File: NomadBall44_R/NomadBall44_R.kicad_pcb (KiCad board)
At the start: 2 copper layers, 144.8 x 96.5 mm, 48 parts, among them SW1 SW_Push, SW10 SW_Push, SW11 SW_Push, SW12 SW_Push, SW13 SW_Push, SW14 SW_Push, SW15 SW_Push, SW16 SW_Push, SW17 SW_Push, SW18 SW_Push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

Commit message: pmw3610のコネクタの位置を微調整
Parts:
- BT1: moved to B.Cu
- moved SW11 99.5 mm to (139.6, 59.1)
- moved SW17 99.5 mm to (139.6, 78.3)
- moved SW22 99.5 mm to (139.6, 97.4)
- moved SW5 99.5 mm to (139.6, 39.9)
- moved D14 99.5 mm to (73.2, 64.9)
- moved D16 99.5 mm to (111.6, 67.5)
- moved D20 99.5 mm to (45.0, 95.5)
- moved D8 99.5 mm to (73.2, 45.7)
- moved SW1 99.5 mm to (63.0, 34.0)
- moved SW13 99.5 mm to (63.0, 72.3)
- moved SW20 99.5 mm to (54.7, 99.1)
- moved SW7 99.5 mm to (63.0, 53.1)
- moved D1 99.5 mm to (54.0, 28.7)
- moved D10 99.5 mm to (111.6, 48.3)
- moved D11 99.5 mm to (130.7, 53.9)
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
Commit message: スライドスイッチとロータリーエンコーダーの位置を微修正
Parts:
- moved D21 66.2 mm to (97.9, 90.2)
- moved SW23 58.0 mm to (87.6, 84.9)
- moved SW21 57.6 mm to (87.9, 97.3)
- moved U1 56.2 mm to (95.4, 60.3)
- moved D14 56.2 mm to (125.5, 85.5)
- moved D18 56.2 mm to (202.1, 93.8)
- moved D19 56.2 mm to (76.7, 123.1)
- moved D7 56.2 mm to (106.3, 68.6)
- moved J1 56.2 mm to (175.3, 116.9)
- moved SW14 56.2 mm to (134.4, 90.7)
- moved SW15 56.2 mm to (153.6, 88.4)
- moved SW17 56.2 mm to (191.9, 99.0)
- moved SW18 56.2 mm to (211.1, 99.0)
- moved SW20 56.2 mm to (107.0, 119.8)
- moved SW22 56.2 mm to (191.9, 118.0)
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
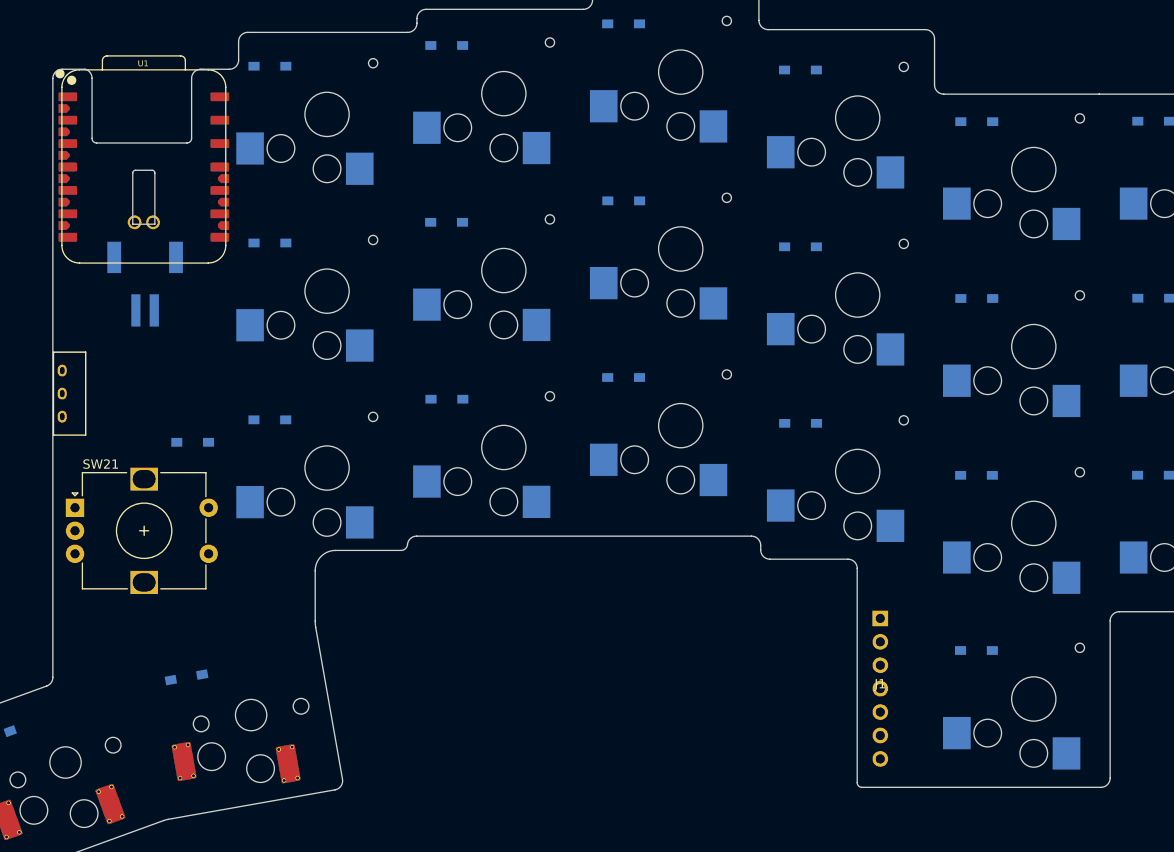
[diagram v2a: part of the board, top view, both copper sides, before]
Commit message: スペーサーを追加
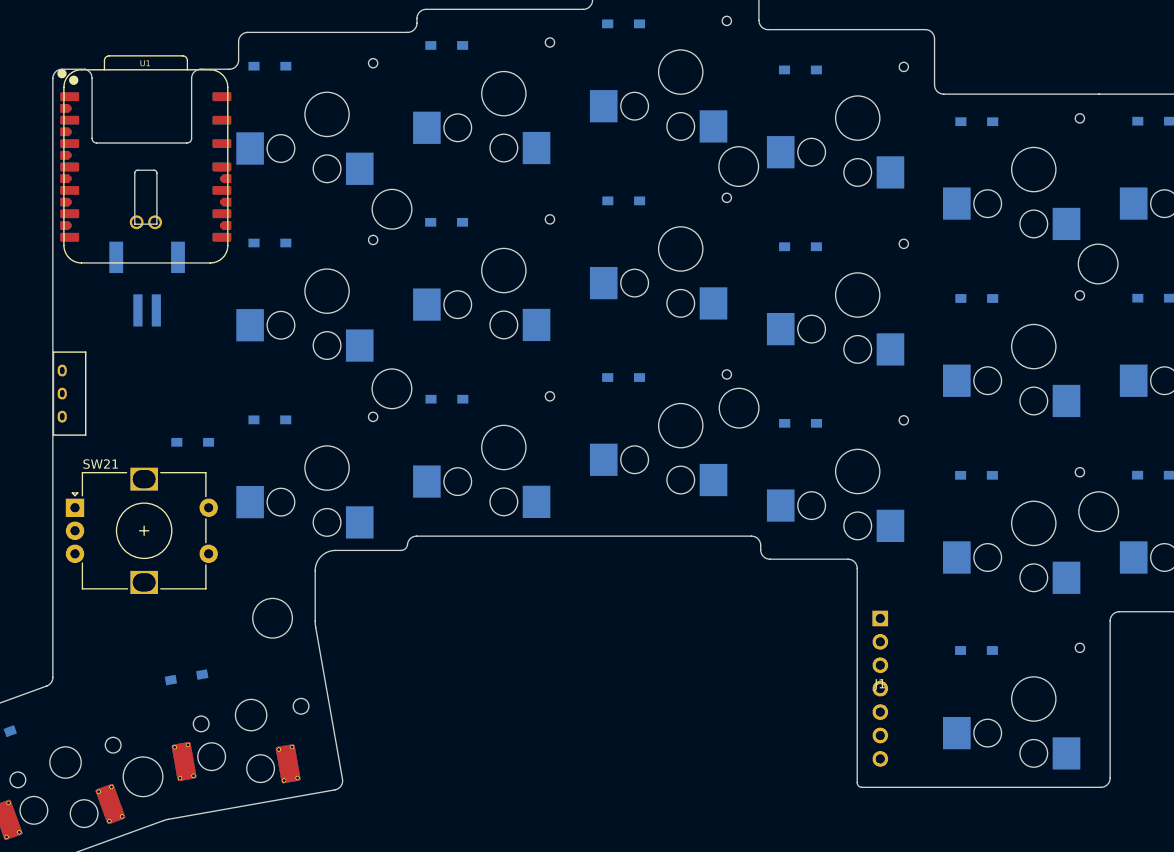
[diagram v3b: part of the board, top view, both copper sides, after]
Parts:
- added REF**: MountingHole_4.3mm_M4, MountingHole:MountingHole_4.3mm_M4, F.Cu at (159.9, 86.5)
- added REF**: MountingHole_4.3mm_M4, MountingHole:MountingHole_4.3mm_M4, F.Cu at (199.0, 97.7)
- added REF**: MountingHole_4.3mm_M4, MountingHole:MountingHole_4.3mm_M4, F.Cu at (122.3, 84.4)
- added REF**: MountingHole_4.3mm_M4, MountingHole:MountingHole_4.3mm_M4, F.Cu at (159.9, 60.3)
- added REF**: MountingHole_4.3mm_M4, MountingHole:MountingHole_4.3mm_M4, F.Cu at (109.3, 109.3)
- added REF**: MountingHole_4.3mm_M4, MountingHole:MountingHole_4.3mm_M4, F.Cu at (198.9, 70.8)
- added REF**: MountingHole_4.3mm_M4, MountingHole:MountingHole_4.3mm_M4, F.Cu at (122.3, 64.9)
- added REF**: MountingHole_4.3mm_M4, MountingHole:MountingHole_4.3mm_M4, F.Cu at (95.3, 126.5)
- moved U1 0.22 mm to (95.6, 60.3)
- moved BT1 0.22 mm to (95.7, 75.9)

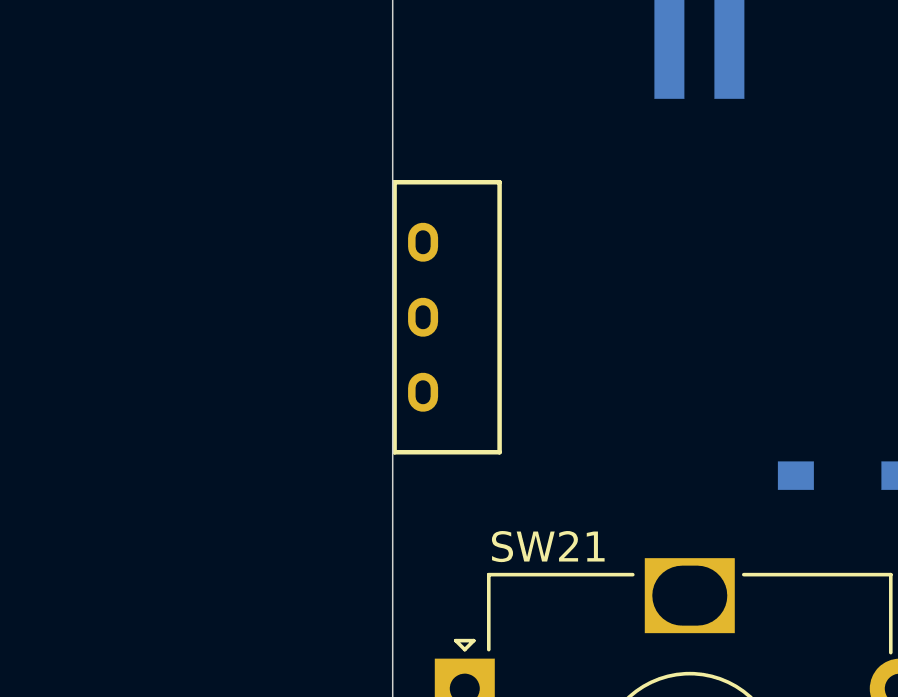
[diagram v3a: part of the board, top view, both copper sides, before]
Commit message: 水平スライドスイッチの位置を修正
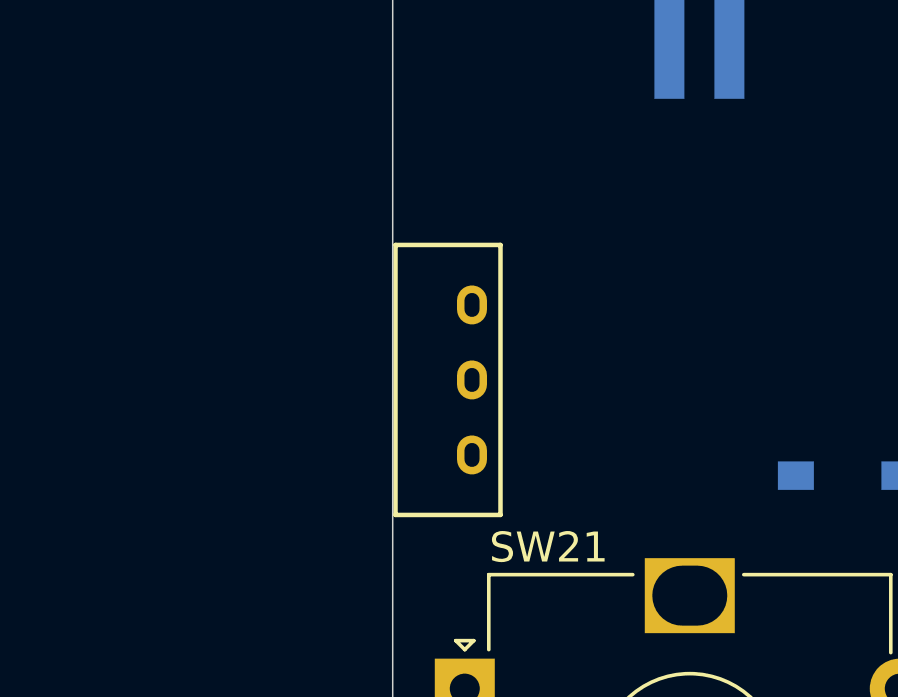
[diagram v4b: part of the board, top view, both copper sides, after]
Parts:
- moved SW23 2.14 mm to (87.1, 87.0), turned to 90 degrees
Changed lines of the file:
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@@
 	(footprint "NomadBall44:TGSW_MSK-12D19"
 		(layer "F.Cu")
-		(at 87.57 84.9 -90)
+		(at 87.1 86.99 90)
 		(property "Reference" "SW23"
 			(at 0 -2 90)
@@
 		(attr through_hole)
 		(fp_line
-			(start -4.5 2)
-			(end -4.5 -1.5)
+			(start 4.5 -1.5)
+			(end 4.5 2)
+			(stroke
+				(width 0.15)
+				(type solid)
+			)
+			(layer "F.SilkS")
+		)
+		(fp_line
+			(start -4.5 -1.5)
+			(end 4.5 -1.5)
 			(stroke
 				(width 0.15)
@@
 		)
 		(fp_line
-			(start -4.5 -1.5)
-			(end 4.5 -1.5)
-			(stroke
-				(width 0.15)
-				(type solid)
-			)
-			(layer "F.SilkS")
-		)
-		(fp_line
-			(start 4.5 -1.5)
-			(end 4.5 2)
+			(start -4.5 2)
+			(end -4.5 -1.5)
 			(stroke
 				(width 0.15)
@@
 		)
 		(pad "1" thru_hole oval
-			(at -2.5 1.05 270)
+			(at -2.5 1.05 90)
 			(size 1.3 1)
 			(drill oval 0.8 0.5)
@@
 		)
 		(pad "2" thru_hole oval
-			(at 0 1.05 270)
+			(at 0 1.05 90)
 			(size 1.3 1)
 			(drill oval 0.8 0.5)
@@
 		)
 		(pad "3" thru_hole oval
-			(at 2.5 1.05 270)
+			(at 2.5 1.05 90)
 			(size 1.3 1)
 			(drill oval 0.8 0.5)

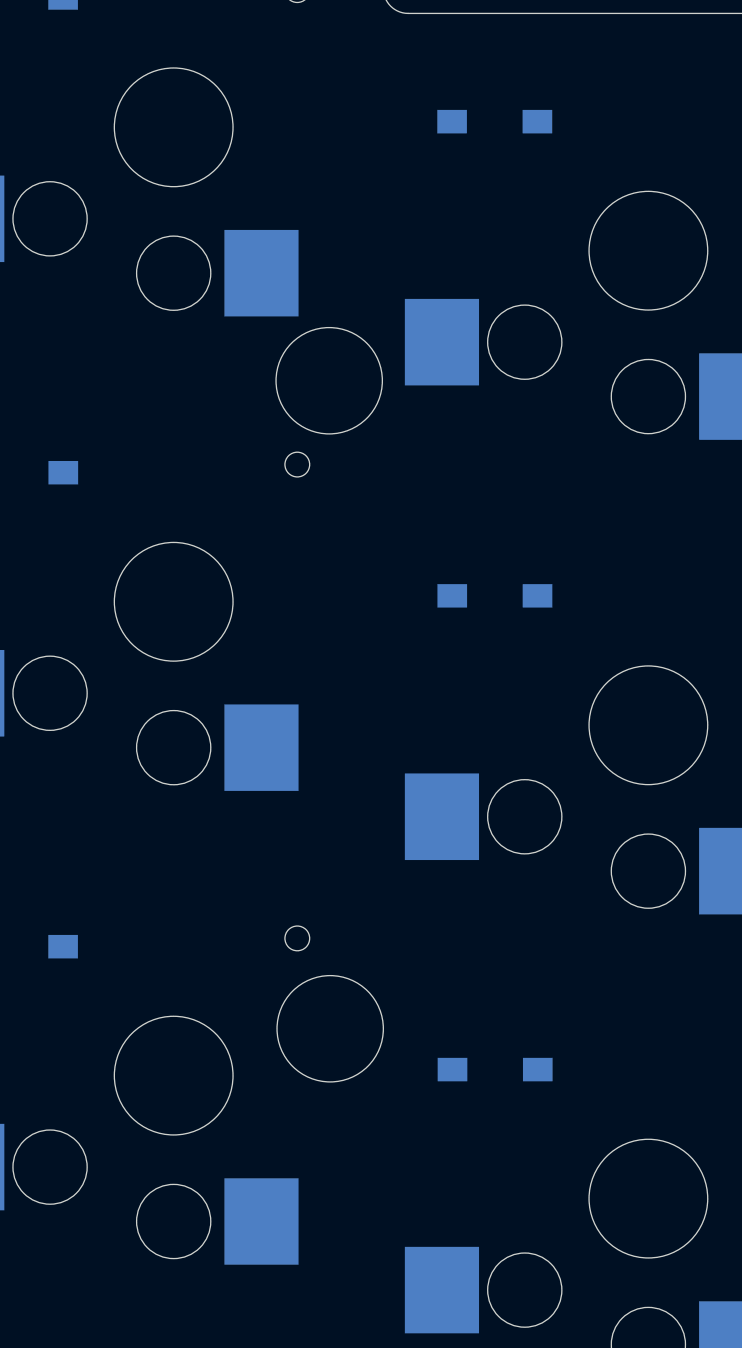
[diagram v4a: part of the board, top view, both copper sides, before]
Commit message: スペーサーの位置を修正
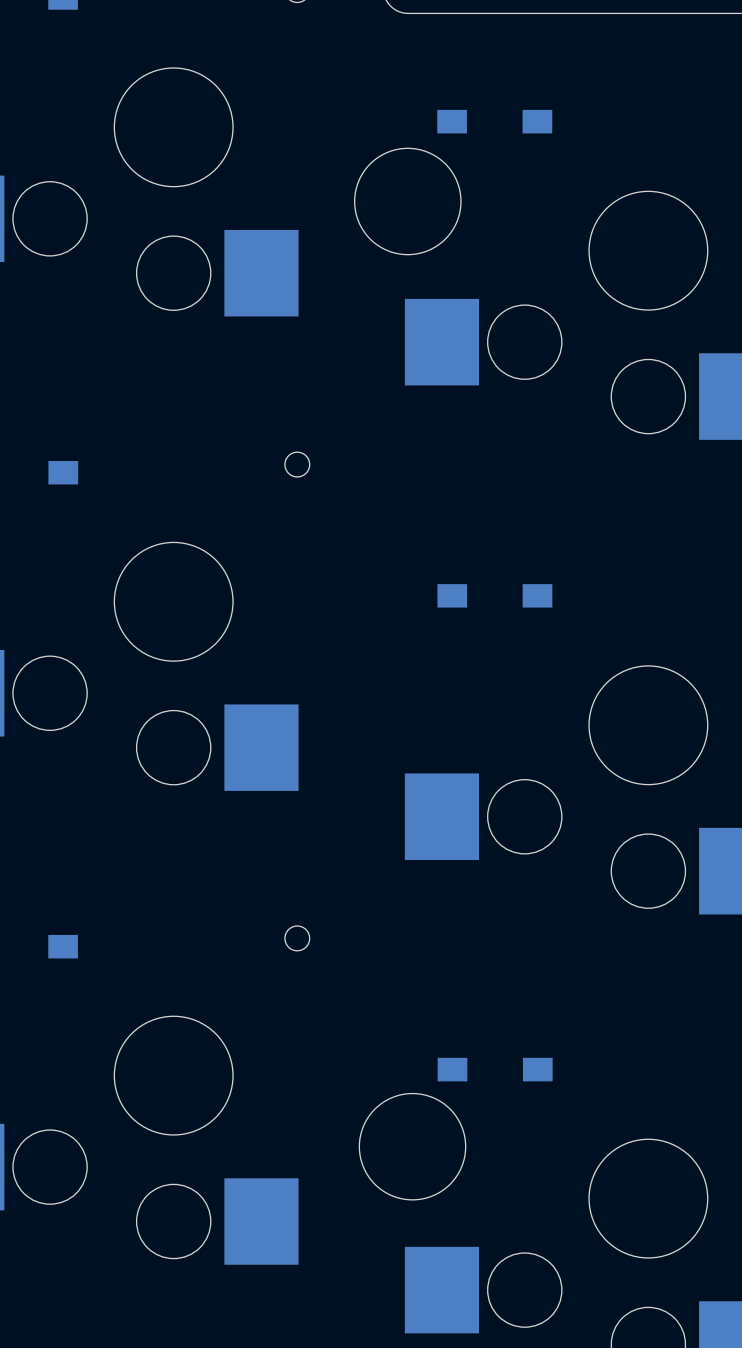
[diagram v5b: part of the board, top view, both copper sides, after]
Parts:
- moved REF** 7.92 mm to (163.1, 53.0)
- moved REF** 5.82 mm to (163.3, 91.2)
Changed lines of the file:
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@@
 	(footprint "MountingHole:MountingHole_4.3mm_M4"
 		(layer "F.Cu")
-		(at 159.95 86.48)
+		(at 163.28 91.25)
 		(descr "Mounting Hole 4.3mm, M4, no annular, generated by kicad-footprint-generator mountinghole.py")
 		(tags "mountinghole M4")
@@
 	(footprint "MountingHole:MountingHole_4.3mm_M4"
 		(layer "F.Cu")
-		(at 159.91 60.27)
+		(at 163.09 53.02)
 		(descr "Mounting Hole 4.3mm, M4, no annular, generated by kicad-footprint-generator mountinghole.py")
 		(tags "mountinghole M4")

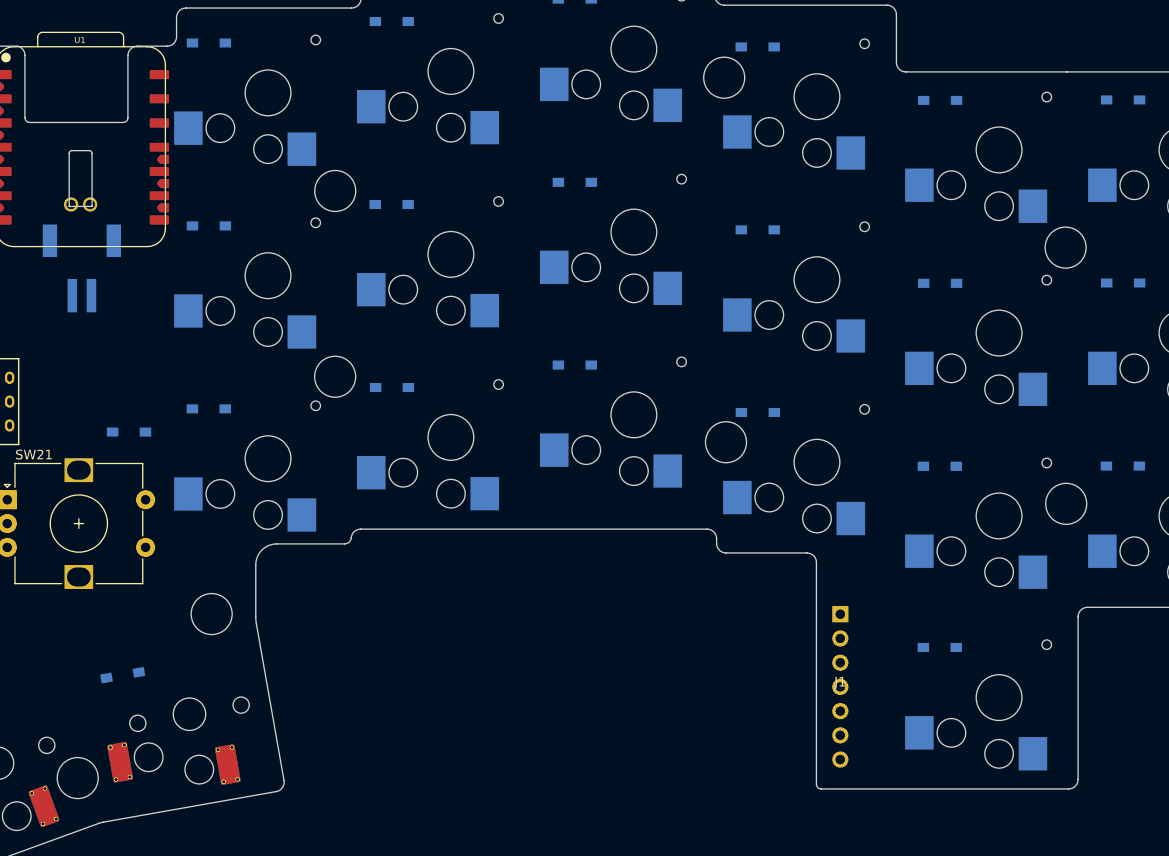
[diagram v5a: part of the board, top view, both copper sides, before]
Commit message: スペーサー用のホール位置を修正
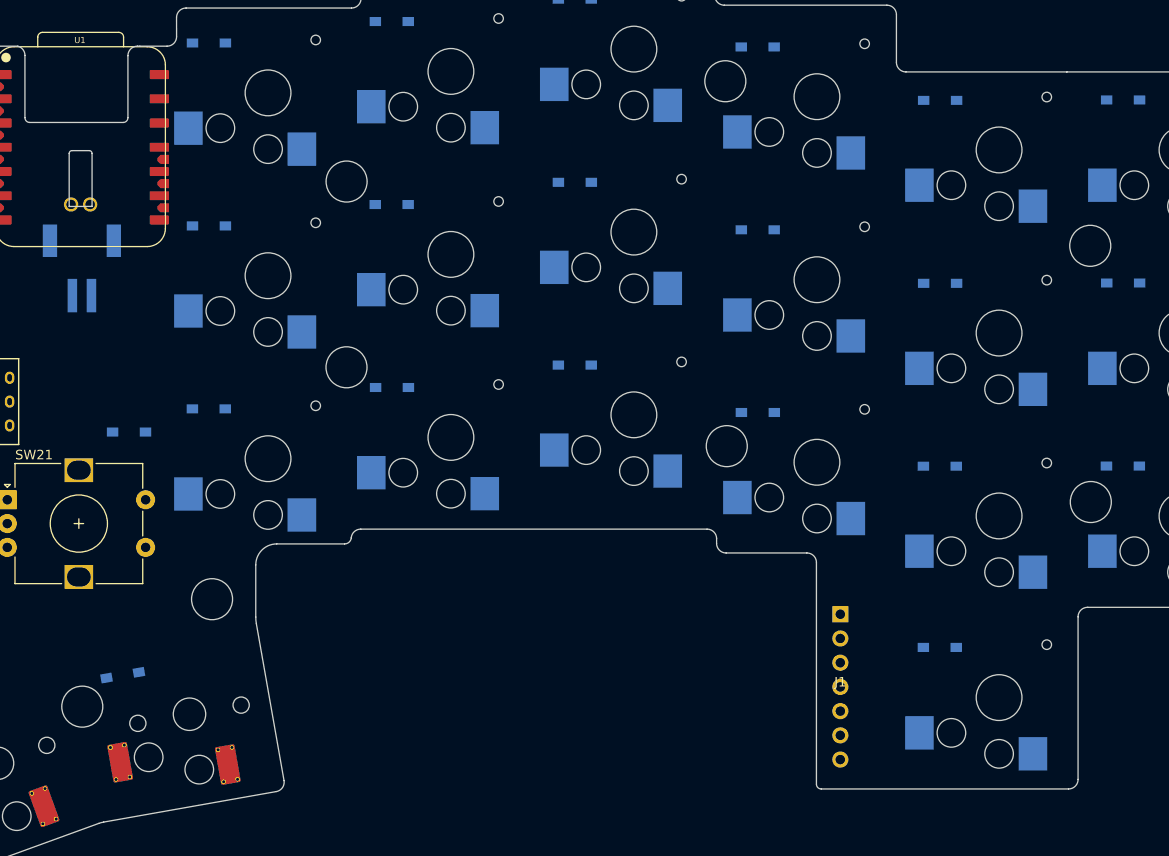
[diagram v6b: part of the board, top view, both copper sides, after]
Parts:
- moved REF** 7.51 mm to (95.8, 119.0)
- moved REF** 2.59 mm to (201.5, 97.5)
- moved REF** 2.59 mm to (201.5, 70.7)
- moved REF** 1.56 mm to (109.4, 107.7)
- moved REF** 1.55 mm to (123.5, 63.9)
- moved REF** 1.55 mm to (123.5, 83.4)
- moved REF** 0.42 mm to (163.4, 91.7)
- moved REF** 0.39 mm to (163.2, 53.4)
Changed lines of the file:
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@@
 	(footprint "MountingHole:MountingHole_4.3mm_M4"
 		(layer "F.Cu")
-		(at 163.28 91.25)
+		(at 163.36 91.66)
 		(descr "Mounting Hole 4.3mm, M4, no annular, generated by kicad-footprint-generator mountinghole.py")
 		(tags "mountinghole M4")
@@
 	(footprint "MountingHole:MountingHole_4.3mm_M4"
 		(layer "F.Cu")
-		(at 198.96 97.71)
+		(at 201.54 97.52)
 		(descr "Mounting Hole 4.3mm, M4, no annular, generated by kicad-footprint-generator mountinghole.py")
 		(tags "mountinghole M4")
@@
 	(footprint "MountingHole:MountingHole_4.3mm_M4"
 		(layer "F.Cu")
-		(at 122.29 84.38)
+		(at 123.48 83.39)
 		(descr "Mounting Hole 4.3mm, M4, no annular, generated by kicad-footprint-generator mountinghole.py")
 		(tags "mountinghole M4")
@@
 	(footprint "MountingHole:MountingHole_4.3mm_M4"
 		(layer "F.Cu")
-		(at 163.09 53.02)
+		(at 163.21 53.39)
 		(descr "Mounting Hole 4.3mm, M4, no annular, generated by kicad-footprint-generator mountinghole.py")
 		(tags "mountinghole M4")
@@
 	(footprint "MountingHole:MountingHole_4.3mm_M4"
 		(layer "F.Cu")
-		(at 109.34 109.27)
+		(at 109.38 107.71)
 		(descr "Mounting Hole 4.3mm, M4, no annular, generated by kicad-footprint-generator mountinghole.py")
 		(tags "mountinghole M4")
@@
 	(footprint "MountingHole:MountingHole_4.3mm_M4"
 		(layer "F.Cu")
-		(at 198.9 70.84)
+		(at 201.48 70.65)
 		(descr "Mounting Hole 4.3mm, M4, no annular, generated by kicad-footprint-generator mountinghole.py")
 		(tags "mountinghole M4")
@@
 	(footprint "MountingHole:MountingHole_4.3mm_M4"
 		(layer "F.Cu")
-		(at 122.3 64.9)
+		(at 123.49 63.91)
 		(descr "Mounting Hole 4.3mm, M4, no annular, generated by kicad-footprint-generator mountinghole.py")
 		(tags "mountinghole M4")
@@
 	(footprint "MountingHole:MountingHole_4.3mm_M4"
 		(layer "F.Cu")
-		(at 95.29 126.47)
+		(at 95.77 118.98)
 		(descr "Mounting Hole 4.3mm, M4, no annular, generated by kicad-footprint-generator mountinghole.py")
 		(tags "mountinghole M4")
